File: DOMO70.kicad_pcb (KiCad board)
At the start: 2 copper layers, 148 parts, among them SW1 Rotary_Encoder_Switch, SW2 Rotary_Encoder_Switch, U1 OLED-SSD1306-OLED-SSD1306-4pi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, U2 proton_c

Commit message: Created speaker footprint/symbol
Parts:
- added D45: 1N4148, cftkb:D_DO-35_SOD27_P5.08mm_Horizontal, F.Cu at (232.4, 71.1)
- added D57: 1N4148, cftkb:D_DO-35_SOD27_P5.08mm_Horizontal, F.Cu at (232.4, 74.7)
- added D74: 1N4148, cftkb:D_DO-35_SOD27_P5.08mm_Horizontal, F.Cu at (241.1, 71.1)
- added MX56: MX-NoLED, MX_Only:MXOnly-1U-NoLED, F.Cu at (221.6, 68.9)
- added U2: AST1109MLTRQ, Buzzer_Beeper:Buzzer_Mallory_AST1109MLTRQ, F.Cu at (240.1, 64.1)
- renumbered D66 to D10, D67 to D11, D68 to D12, D69 to D13, D70 to D14, D71 to D15, D10 to D16, D11 to D17, D12 to D18, D13 to D19, D14 to D20, D15 to D21, D16 to D22, D17 to D23, D18 to D24, D59 to D25, D60 to D26, D61 to D27, D62 to D28, D72 to D29, D63 to D30, D19 to D31, D20 to D32, D21 to D33, D22 to D34, D23 to D35, D24 to D36, D25 to D37, D26 to D38, D51 to D39, D52 to D40, D53 to D41, D54 to D42, D56 to D43, D57 to D44, D27 to D46, D28 to D47, D29 to D48, D30 to D49, D31 to D50, D32 to D51, D33 to D52, D34 to D53, D47 to D54, D48 to D55, D49 to D56, D41 to D58, D50 to D59, D35 to D60, D36 to D61, D37 to D62, D38 to D63, D65 to D64, D39 to D65, D40 to D66, D58 to D67, D55 to D68, D46 to D69, D42 to D70, D43 to D71, D44 to D72, D45 to D73, MX66 to MX10, MX67 to MX11, MX68 to MX12, MX69 to MX13, MX70 to MX14, MX71 to MX15, MX10 to MX16, MX11 to MX17, MX12 to MX18, MX13 to MX19, MX14 to MX20, MX15 to MX21, MX16 to MX22, MX17 to MX23, MX18 to MX24, MX59 to MX25, MX60 to MX26, MX61 to MX27, MX62 to MX28, MX72 to MX29, MX63 to MX30, MX19 to MX31, MX20 to MX32, MX21 to MX33, MX22 to MX34, MX23 to MX35, MX24 to MX36, MX25 to MX37, MX26 to MX38, MX51 to MX39, MX52 to MX40, MX53 to MX41, MX54 to MX42, MX56 to MX43, MX57 to MX44, MX27 to MX45, MX28 to MX46, MX29 to MX47, MX30 to MX48, MX31 to MX49, MX32 to MX50, MX33 to MX51, MX34 to MX52, MX47 to MX53, MX48 to MX54, MX49 to MX55, MX41 to MX57, MX50 to MX58, MX35 to MX59, MX36 to MX60, MX37 to MX61, MX38 to MX62, MX65 to MX63, MX39 to MX64, MX40 to MX65, MX58 to MX66, MX55 to MX67, MX46 to MX68, MX42 to MX69, MX43 to MX70, MX44 to MX71, MX45 to MX72, U2 to U3
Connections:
- D10 pad 1: ROW8 -> ROW0
- D11 pad 1: ROW8 -> ROW0
- D12 pad 1: ROW8 -> ROW0
- D13 pad 1: ROW8 -> ROW0
- D14 pad 1: ROW8 -> ROW0
- D15 pad 1: ROW8 -> ROW0
- D25 pad 1: ROW7 -> ROW1
- D26 pad 1: ROW7 -> ROW1
- D27 pad 1: ROW7 -> ROW1
- D28 pad 1: ROW7 -> ROW1
- D29 pad 1: ROW8 -> ROW1
- D30 pad 1: ROW7 -> ROW1
- D39 pad 1: ROW6 -> ROW2
- D40 pad 1: ROW6 -> ROW2
- D41 pad 1: ROW6 -> ROW2
- D42 pad 1: ROW6 -> ROW2
- D43 pad 1: ROW6 -> ROW2
- D44 pad 1: ROW6 -> ROW2
- D54 pad 1: ROW5 -> ROW3
- D55 pad 1: ROW5 -> ROW3
- D56 pad 1: ROW5 -> ROW3
- D58 pad 1: ROW4 -> ROW3
- D59 pad 1: ROW5 -> ROW3
- D64 pad 1: ROW7 -> ROW4
- D64 pad 2: Net-(D65-Pad2) (its old number) -> Net-(D64-Pad2)
- D67 pad 1: ROW6 -> ROW4
- D68 pad 1: ROW6 -> ROW4
- D69 pad 1: ROW5 -> ROW4
- D71 pad 1: ROW5 -> ROW4
- D72 pad 1: ROW5 -> ROW4
- D73 pad 1: ROW5 -> ROW4
- MX10 pad 1: COL0 -> COL9
- MX11 pad 1: COL1 -> COL10
- MX12 pad 1: COL2 -> COL11
- MX13 pad 1: COL3 -> COL12
- MX14 pad 1: COL4 -> COL13
- MX15 pad 1: COL5 -> COL14
- MX25 pad 1: COL0 -> COL9
- MX26 pad 1: COL1 -> COL10
- MX27 pad 1: COL2 -> COL11
- MX28 pad 1: COL3 -> COL12
- MX29 pad 1: COL6 -> COL13
- MX30 pad 1: COL4 -> COL14
- MX39 pad 1: COL0 -> COL8
- MX40 pad 1: COL1 -> COL9
- MX41 pad 1: COL2 -> COL10
- MX42 pad 1: COL3 -> COL11
- MX43 pad 1: COL5 -> COL12
- MX44 pad 1: COL6 -> COL13
- MX53 pad 1: COL4 -> COL8
- MX54 pad 1: COL5 -> COL9
- MX55 pad 1: COL6 -> COL10
- MX57 pad 1: COL6 -> COL12
- MX58 pad 1: COL7 -> COL13
- MX63 pad 1: COL6 -> COL4
- MX63 pad 2: Net-(D65-Pad2) (its old number) -> Net-(D64-Pad2)
- MX64 pad 1: COL4 -> COL5
- MX65 pad 1: COL5 -> COL6
- MX66 pad 1: COL7 -> Net-(MX66-Pad1)
- MX67 pad 1: COL4 -> Net-(MX67-Pad1)
- MX68 pad 1: COL3 -> Net-(MX68-Pad1)
- MX69 pad 1: COL7 -> COL10
- MX70 pad 1: COL0 -> COL11
- MX71 pad 1: COL1 -> COL12
- MX72 pad 1: COL2 -> COL13
- SW1 pad S1: ROW7 -> Net-(D45-Pad2)
- SW1 pad S2: COL7 -> COL14
- SW2 pad S1: ROW8 -> Net-(D74-Pad2)
- SW2 pad S2: COL7 -> COL14
- U3 pad A10: Net-(U2-PadA10) -> COL13
- U3 pad A13: COL3 -> COL7
- U3 pad A14: COL2 -> COL6
- U3 pad A4: Net-(U2-PadA4) -> SPK
- U3 pad A8: Net-(U2-PadA8) -> COL8
- U3 pad A9: Net-(U2-PadA9) -> COL14
- U3 pad B10: ROW8 -> COL3
- U3 pad B11: COL0 -> COL4
- U3 pad B12: COL1 -> COL5
- U3 pad B14: ROW5 -> COL0
- U3 pad B15: ROW6 -> COL1
- U3 pad B2: COL7 -> COL9
- U3 pad B3: COL6 -> COL10
- U3 pad B4: COL5 -> COL11
- U3 pad B5: COL4 -> COL12
- U3 pad B9: ROW7 -> COL2
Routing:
- net GND: track 0.00 -> 1.66 mm

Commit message: Added routing
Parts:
- removed the D64 at (148.0, -58.9)
- removed the D64 at (106.6, -64.8)
- removed D73, D74: 1N4148, cftkb:D_DO-35_SOD27_P5.08mm_Horizontal
- removed the MX64 at (-75.9, -27.0)
- removed the MX64 at (-175.7, -0.44)
- added D64: 1N4148, cftkb:D_DO-35_SOD27_P5.08mm_Horizontal, B.Cu at (259.6, 130.2)
- added DE1: 1N4148, cftkb:D_DO-35_SOD27_P5.08mm_Horizontal, B.Cu at (354.0, 73.0)
- added DE2: 1N4148, cftkb:D_DO-35_SOD27_P5.08mm_Horizontal, B.Cu at (326.2, 73.0)
- added MX64: MX-NoLED, MX_Only:MXOnly-1.25U-NoLED, F.Cu at (250.0, 126.2)
- added MX_14: ExtraMX, MX_Only:MXOnly-2U-NoLED, F.Cu at (290.5, 50.0)
- added MX_29: ExtraMX, MX_Only:MXOnly-ISO-ReversedStabilizers, F.Cu at (297.7, 78.6)
- added MX_31: ExtraMX, MX_Only:MXOnly-1.25U-NoLED, F.Cu at (35.7, 88.1)
- added MX_43: ExtraMX, MX_Only:MXOnly-1U-NoLED, F.Cu at (276.2, 88.1)
- added MX_56: ExtraMX, MX_Only:MXOnly-1.75U-NoLED, F.Cu at (273.8, 107.2)
- added MX_59: ExtraMX, MX_Only:MXOnly-1.5U-NoLED, F.Cu at (38.1, 126.2)
- added MX_60: ExtraMX, MX_Only:MXOnly-1U-NoLED, F.Cu at (61.9, 126.2)
- added MX_61: ExtraMX, MX_Only:MXOnly-1.5U-NoLED, F.Cu at (85.7, 126.2)
- added MX_62: ExtraMX, MX_Only:MXOnly-7U-ReversedStabilizers-NoLED, F.Cu at (166.7, 126.2)
- added MX_64: ExtraMX, MX_Only:MXOnly-1.5U-NoLED, F.Cu at (247.7, 126.2)
- added MX_65: ExtraMX, MX_Only:MXOnly-1U-NoLED, F.Cu at (271.5, 126.2)
- added MX_66: ExtraMX, MX_Only:MXOnly-1.5U-NoLED, F.Cu at (295.3, 126.2)
- added U4: AST1109MLTRQ, Buzzer_Beeper:Buzzer_Mallory_AST1109MLTRQ, B.Cu at (192.1, 126.2)
- D24, D45, D57, D9: moved to B.Cu
- MX29: footprint MX_Only:MXOnly-1U-NoLED -> MX_Only:MXOnly-1.5U-NoLED
- MX31: footprint MX_Only:MXOnly-1U-NoLED -> MX_Only:MXOnly-1.75U-NoLED
- MX43, MX45: footprint MX_Only:MXOnly-1U-NoLED -> MX_Only:MXOnly-2.25U-NoLED
- MX56: footprint MX_Only:MXOnly-1U-NoLED -> MX_Only:MXOnly-2.75U-NoLED
- MX59, MX60, MX61, MX63, MX65, MX66: footprint MX_Only:MXOnly-1U-NoLED -> MX_Only:MXOnly-1.25U-NoLED
- MX62: footprint MX_Only:MXOnly-1U-NoLED -> MX_Only:MXOnly-6.25U-ReversedStabilizers-NoLED
- U1: value OLED-SSD1306-OLED-SSD1306-4pin-128x32 -> proton_c; footprint OLED-SSD1306-4pin-128x32:OLED-1306-Supports -> proton_c:proton_c; moved to B.Cu
- U2: value AST1109MLTRQ -> OLED-SSD1306-OLED-SSD1306-4pin-128x32; footprint Buzzer_Beeper:Buzzer_Mallory_AST1109MLTRQ -> OLED-SSD1306-4pin-128x32:OLED-1306-Supports
- U3: value proton_c -> AST1109MLTRQ; footprint proton_c:proton_c -> Buzzer_Beeper:Buzzer_Mallory_AST1109MLTRQ; moved to B.Cu
- moved MX58 511.9 mm to (357.2, 88.1)
- moved MX69 504.7 mm to (357.2, 107.2)
- moved MX15 475.8 mm to (300.0, 50.0)
- moved MX66 460.4 mm to (297.7, 126.2)
- moved D24 457.0 mm to (203.2, 73.0), turned to 90 degrees
- moved MX44 454.8 mm to (338.1, 88.1)
- moved MX57 450.0 mm to (300.0, 107.2)
- moved D9 448.4 mm to (193.7, 54.0), turned to 90 degrees
- moved MX43 444.5 mm to (288.1, 88.1)
- moved MX67 440.3 mm to (319.1, 107.2)
- moved MX68 439.2 mm to (338.1, 107.2)
- moved MX9 435.9 mm to (185.7, 50.0)
- moved MX24 434.8 mm to (195.3, 69.1)
- moved MX29 422.7 mm to (295.3, 69.1)
- moved MX30 420.6 mm to (319.1, 88.1)
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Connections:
- D45 pad 1: ROW2 -> ROW3
- D59 pad 1: ROW3 -> ROW4
- MX45 pad 2: Net-(D46-Pad2) -> Net-(D45-Pad2)
- MX46 pad 2: Net-(D47-Pad2) -> Net-(D46-Pad2)
- MX47 pad 2: Net-(D48-Pad2) -> Net-(D47-Pad2)
- MX48 pad 2: Net-(D49-Pad2) -> Net-(D48-Pad2)
- MX49 pad 2: Net-(D50-Pad2) -> Net-(D49-Pad2)
- MX50 pad 2: Net-(D51-Pad2) -> Net-(D50-Pad2)
- MX51 pad 2: Net-(D52-Pad2) -> Net-(D51-Pad2)
- MX52 pad 2: Net-(D53-Pad2) -> Net-(D52-Pad2)
- MX53 pad 2: Net-(D54-Pad2) -> Net-(D53-Pad2)
- MX54 pad 2: Net-(D55-Pad2) -> Net-(D54-Pad2)
- MX55 pad 2: Net-(D56-Pad2) -> Net-(D55-Pad2)
- MX56 pad 2: Net-(D57-Pad2) -> Net-(D56-Pad2)
- MX57 pad 2: Net-(D58-Pad2) -> Net-(D57-Pad2)
- MX58 pad 2: Net-(D59-Pad2) -> Net-(D58-Pad2)
- MX59 pad 2: Net-(D60-Pad2) -> Net-(D59-Pad2)
- MX60 pad 2: Net-(D61-Pad2) -> Net-(D60-Pad2)
- MX61 pad 2: Net-(D62-Pad2) -> Net-(D61-Pad2)
- MX62 pad 2: Net-(D63-Pad2) -> Net-(D62-Pad2)
- MX63 pad 2: Net-(D64-Pad2) -> Net-(D63-Pad2)
- MX65 pad 2: Net-(D66-Pad2) -> Net-(D65-Pad2)
- MX66 pad 1: Net-(MX66-Pad1) -> COL7
- MX66 pad 2: Net-(D67-Pad2) -> Net-(D66-Pad2)
- MX67 pad 1: Net-(MX67-Pad1) -> COL8
- MX67 pad 2: Net-(D68-Pad2) -> Net-(D67-Pad2)
- MX68 pad 1: Net-(MX68-Pad1) -> COL9
- MX68 pad 2: Net-(D69-Pad2) -> Net-(D68-Pad2)
- MX69 pad 2: Net-(D70-Pad2) -> Net-(D69-Pad2)
- MX70 pad 2: Net-(D71-Pad2) -> Net-(D70-Pad2)
- MX71 pad 2: Net-(D72-Pad2) -> Net-(D71-Pad2)
- MX72 pad 2: Net-(D73-Pad2) -> Net-(D72-Pad2)
- SW1 pad S1: Net-(D45-Pad2) -> Net-(DE1-Pad2)
- U2 pad 1: SPK -> SDA
- U2 pad 2: GND -> SCL
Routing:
- net ROW4: track 0.00 -> 452.4 mm, vias 0 -> 1
- net COL0: track 0.00 -> 394.1 mm
- net COL1: track 0.00 -> 370.4 mm
- net ROW2: track 0.00 -> 363.4 mm, vias 0 -> 1
- net ROW3: track 0.00 -> 354.7 mm, vias 0 -> 1
- net COL2: track 0.00 -> 346.8 mm
- net ROW1: track 0.00 -> 321.6 mm, vias 0 -> 2
- net COL3: track 0.00 -> 317.9 mm, vias 0 -> 1
- net COL4: track 0.00 -> 299.7 mm, vias 0 -> 1
- net ROW0: track 0.00 -> 295.5 mm
- net GND: track 1.66 -> 285.5 mm, vias 0 -> 1
- net COL5: track 0.00 -> 278.0 mm
- net SPK: track 0.00 -> 263.6 mm, vias 0 -> 2
- net COL6: track 0.00 -> 258.2 mm
- net COL7: track 0.00 -> 244.0 mm, vias 0 -> 1
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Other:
- board outline added: 342.9 x 95.2 mm
- net class Default: clearance 0.2 -> 0.3
- net class Power added: clearance 0.3, trace_width 0.381, via_dia 0.8, via_drill 0.4
- rule trace_clearance: 0.2 -> 0.3

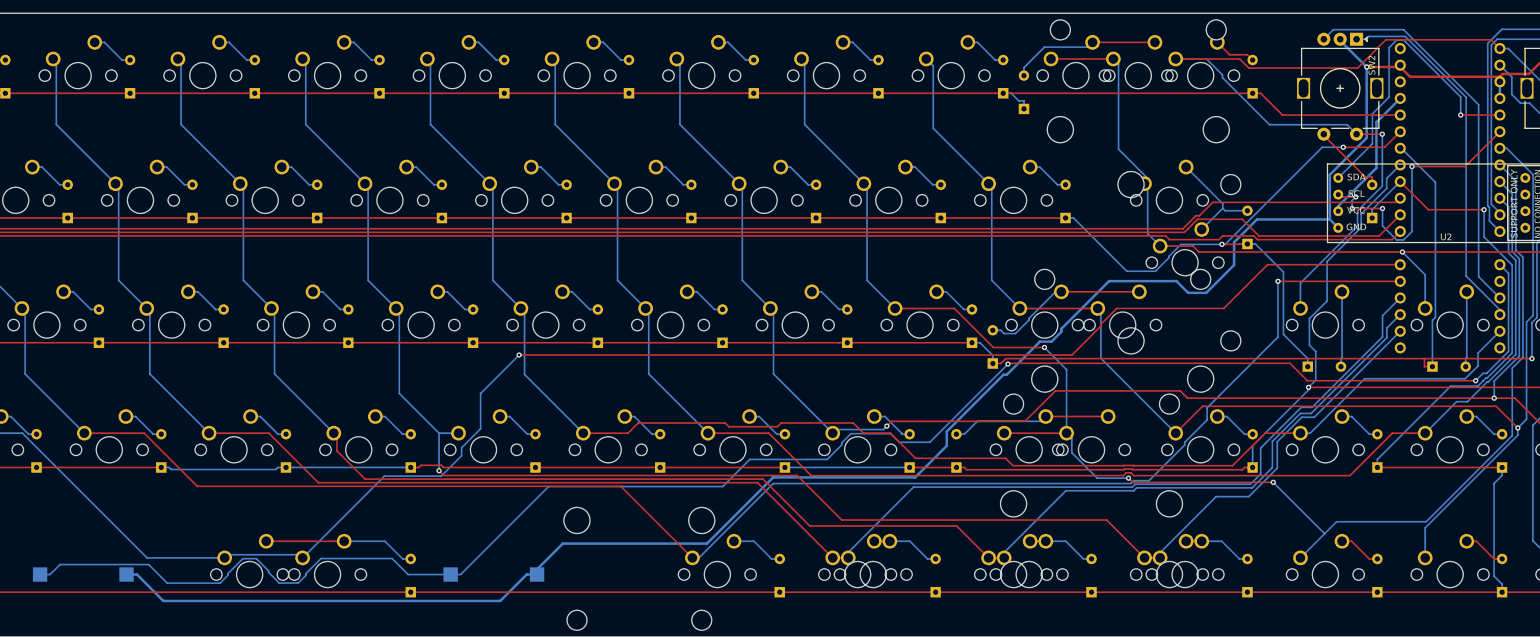
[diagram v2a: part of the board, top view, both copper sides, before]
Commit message: Added more routing
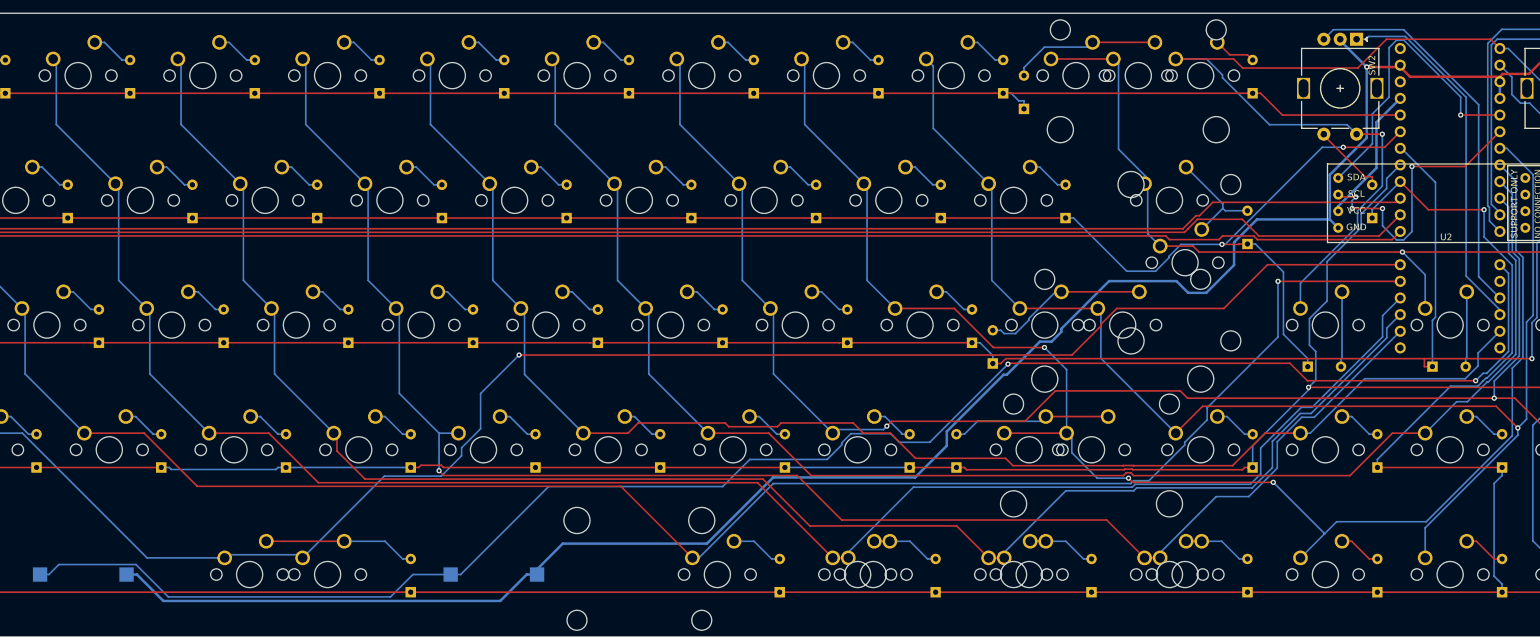
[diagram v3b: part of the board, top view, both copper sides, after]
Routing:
- net SPK: track 263.6 -> 259.8 mm
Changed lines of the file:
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@@
     (thickness 1.6)
     (drawings 8)
-    (tracks 979)
+    (tracks 968)
     (zones 0)
     (modules 164)
@@
   (segment (start 347.0185 45.8688) (end 345.738 45.8688) (width 0.25) (layer B.Cu) (net 100))
   (via (at 327.7822 58.95) (size 0.8) (layers F.Cu B.Cu) (net 100))
-  (segment (start 344.4036 44.5344) (end 345.738 45.8688) (width 0.25) (layer F.Cu) (net 100))
-  (segment (start 328.3236 44.5344) (end 344.4036 44.5344) (width 0.25) (layer F.Cu) (net 100))
-  (segment (start 324.007999 48.850001) (end 328.3236 44.5344) (width 0.25) (layer F.Cu) (net 100))
-  (segment (start 307.386999 48.850001) (end 324.007999 48.850001) (width 0.25) (layer F.Cu) (net 100))
-  (segment (start 306.003198 47.4662) (end 307.386999 48.850001) (width 0.25) (layer F.Cu) (net 100))
-  (segment (start 296.228 47.4662) (end 306.003198 47.4662) (width 0.25) (layer F.Cu) (net 100))
+  (segment (start 344.888001 45.018801) (end 345.738 45.8688) (width 0.25) (layer F.Cu) (net 100))
+  (segment (start 344.3192 44.45) (end 344.888001 45.018801) (width 0.25) (layer F.Cu) (net 100))
+  (segment (start 328.424298 44.45) (end 344.3192 44.45) (width 0.25) (layer F.Cu) (net 100))
+  (segment (start 324.024297 48.850001) (end 328.424298 44.45) (width 0.25) (layer F.Cu) (net 100))
+  (segment (start 306.456252 48.850001) (end 324.024297 48.850001) (width 0.25) (layer F.Cu) (net 100))
+  (segment (start 305.072451 47.4662) (end 306.456252 48.850001) (width 0.25) (layer F.Cu) (net 100))
+  (segment (start 296.228 47.4662) (end 305.072451 47.4662) (width 0.25) (layer F.Cu) (net 100))
   (segment (start 342.0369 96.6082) (end 316.3395 96.6082) (width 0.25) (layer F.Cu) (net 101))
   (segment (start 316.3395 96.6082) (end 313.672 93.9407) (width 0.25) (layer F.Cu) (net 101))
@@
   (segment (start 258.6659 106.0057) (end 270.6053 94.0663) (width 0.25) (layer B.Cu) (net 101))
   (segment (start 185.488 126.206) (end 187.0133 126.206) (width 0.25) (layer B.Cu) (net 101))
-  (segment (start 124.3063 126.206) (end 125.8316 124.6807) (width 0.25) (layer B.Cu) (net 101))
-  (segment (start 125.8316 124.6807) (end 139.3616 124.6807) (width 0.25) (layer B.Cu) (net 101))
-  (segment (start 139.3616 124.6807) (end 142.1996 127.5187) (width 0.25) (layer B.Cu) (net 101))
-  (segment (start 142.1996 127.5187) (end 150.2764 127.5187) (width 0.25) (layer B.Cu) (net 101))
-  (segment (start 150.2764 127.5187) (end 151.4687 126.3264) (width 0.25) (layer B.Cu) (net 101))
-  (segment (start 151.4687 126.3264) (end 151.4687 126.0715) (width 0.25) (layer B.Cu) (net 101))
-  (segment (start 151.4687 126.0715) (end 153.7538 123.7864) (width 0.25) (layer B.Cu) (net 101))
-  (segment (start 153.7538 123.7864) (end 155.8105 123.7864) (width 0.25) (layer B.Cu) (net 101))
-  (segment (start 155.8105 123.7864) (end 157.6853 125.6612) (width 0.25) (layer B.Cu) (net 101))
-  (segment (start 157.6853 125.6612) (end 157.6853 125.8846) (width 0.25) (layer B.Cu) (net 101))
-  (segment (start 157.6853 125.8846) (end 159.3071 127.5064) (width 0.25) (layer B.Cu) (net 101))
-  (segment (start 159.3071 127.5064) (end 162.21 127.5064) (width 0.25) (layer B.Cu) (net 101))
-  (segment (start 162.21 127.5064) (end 163.3757 126.3407) (width 0.25) (layer B.Cu) (net 101))
-  (segment (start 163.3757 126.3407) (end 163.3757 126.0715) (width 0.25) (layer B.Cu) (net 101))
-  (segment (start 163.3757 126.0715) (end 165.6896 123.7576) (width 0.25) (layer B.Cu) (net 101))
-  (segment (start 165.6896 123.7576) (end 176.5386 123.7576) (width 0.25) (layer B.Cu) (net 101))
-  (segment (start 176.5386 123.7576) (end 178.987 126.206) (width 0.25) (layer B.Cu) (net 101))
-  (segment (start 178.987 126.206) (end 185.488 126.206) (width 0.25) (layer B.Cu) (net 101))
   (segment (start 342.0369 96.6082) (end 343.1673 95.4778) (width 0.25) (layer B.Cu) (net 101))
   (segment (start 343.1673 95.4778) (end 343.7235 95.4778) (width 0.25) (layer B.Cu) (net 101))
@@
   (segment (start 347.059 92.1423) (end 347.059 80.2098) (width 0.25) (layer B.Cu) (net 101))
   (segment (start 347.059 80.2098) (end 345.738 78.8888) (width 0.25) (layer B.Cu) (net 101))
-  (segment (start 122.781 126.206) (end 124.3063 126.206) (width 0.25) (layer B.Cu) (net 101))
   (via (at 342.0369 96.6082) (size 0.8) (layers F.Cu B.Cu) (net 101))
   (via (at 270.6053 94.0663) (size 0.8) (layers F.Cu B.Cu) (net 101))
+  (segment (start 124.131 126.206) (end 122.781 126.206) (width 0.25) (layer B.Cu) (net 101))
+  (segment (start 125.656001 124.680999) (end 124.131 126.206) (width 0.25) (layer B.Cu) (net 101))
+  (segment (start 137.421001 124.680999) (end 125.656001 124.680999) (width 0.25) (layer B.Cu) (net 101))
+  (segment (start 142.364292 129.62429) (end 137.421001 124.680999) (width 0.25) (layer B.Cu) (net 101))
+  (segment (start 176.303708 129.62429) (end 142.364292 129.62429) (width 0.25) (layer B.Cu) (net 101))
+  (segment (start 179.721998 126.206) (end 176.303708 129.62429) (width 0.25) (layer B.Cu) (net 101))
+  (segment (start 185.488 126.206) (end 179.721998 126.206) (width 0.25) (layer B.Cu) (net 101))
   (segment (start 354.012 66.675) (end 354.012 59.981) (width 0.25) (layer B.Cu) (net 102))
   (segment (start 354.012 59.981) (end 352.981 58.95) (width 0.25) (layer B.Cu) (net 102))

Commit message: Updating who-knows-what
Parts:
- moved D72 56.8 mm to (310.4, 145.3)
- moved D58 53.5 mm to (314.3, 108.7), turned to 0 degrees
- moved D68 53.5 mm to (295.3, 127.8), turned to 0 degrees
- moved D69 53.5 mm to (314.3, 127.8), turned to 0 degrees
- moved D67 53.5 mm to (276.2, 127.8), turned to 0 degrees
- moved D30 41.4 mm to (276.2, 108.7)
- moved D44 41.4 mm to (295.3, 108.7)
- moved D65 40.9 mm to (244.5, 142.9)
- moved MX56 40.9 mm to (244.5, 119.9)
- moved D14 40.9 mm to (234.2, 69.1)
- moved D29 40.9 mm to (268.3, 89.7)
- moved D36 40.9 mm to (111.9, 104.8)
- moved D38 40.9 mm to (150.0, 104.8)
- moved D40 40.9 mm to (188.1, 104.8)
- moved D41 40.9 mm to (207.2, 104.8)
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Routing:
- net ROW4: track 452.4 -> 0.00 mm, vias 1 -> 0
- net COL0: track 394.1 -> 0.00 mm
- net COL1: track 370.4 -> 0.00 mm
- net ROW2: track 363.4 -> 0.00 mm, vias 1 -> 0
- net ROW3: track 354.7 -> 0.00 mm, vias 1 -> 0
- net COL2: track 346.8 -> 0.00 mm
- net ROW1: track 321.6 -> 0.00 mm, vias 2 -> 0
- net COL3: track 317.9 -> 0.00 mm, vias 1 -> 0
- net COL4: track 299.7 -> 0.00 mm, vias 1 -> 0
- net ROW0: track 295.5 -> 0.00 mm
- net GND: track 285.5 -> 0.00 mm, vias 1 -> 0
- net COL5: track 278.0 -> 0.00 mm
- net SPK: track 259.8 -> 0.00 mm, vias 2 -> 0
- net COL6: track 258.2 -> 0.00 mm
- net COL7: track 244.0 -> 0.00 mm, vias 1 -> 0
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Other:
- board size 342.9 x 95.2 mm -> 342.9 x 95.3 mm
- board text added: "Designed By Dom Ruggeri 2019"

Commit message: Added routes, graphics
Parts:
- added G***: LOGO, Images:BeezerBike, F.Cu at (288.9, 95.2)
- added G***: LOGO, Images:BeezerWindowNeg, B.Cu at (135.6, 80.6)
- moved D30 24.5 mm to (265.5, 86.7)
- moved D44 24.5 mm to (284.5, 86.7)
- moved D58 24.4 mm to (315.5, 84.3), turned to 90 degrees
- moved D67 24.4 mm to (277.4, 103.4), turned to 90 degrees
- moved D68 24.4 mm to (296.4, 103.4), turned to 90 degrees
- moved D69 24.4 mm to (315.5, 103.4), turned to 90 degrees
- moved D72 23.4 mm to (315.5, 122.4)
- moved MX29 23.1 mm to (245.6, 61.3)
- moved D57 23.1 mm to (258.3, 103.4)
- moved D70 23.1 mm to (277.4, 122.4)
- moved MX30 23.1 mm to (269.4, 80.4)
- moved MX44 23.1 mm to (288.5, 80.4)
- moved MX70 23.1 mm to (269.4, 118.5)
- moved MX71 23.1 mm to (288.5, 118.5)
- moved MX_66 23.1 mm to (245.6, 118.5)
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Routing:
- net ROW4: track 0.00 -> 452.4 mm, vias 0 -> 1
- net COL0: track 0.00 -> 394.1 mm
- net COL1: track 0.00 -> 370.4 mm
- net ROW2: track 0.00 -> 363.4 mm, vias 0 -> 1
- net ROW3: track 0.00 -> 354.7 mm, vias 0 -> 1
- net COL2: track 0.00 -> 346.8 mm
- net ROW1: track 0.00 -> 321.6 mm, vias 0 -> 2
- net COL3: track 0.00 -> 317.9 mm, vias 0 -> 1
- net COL4: track 0.00 -> 299.7 mm, vias 0 -> 1
- net ROW0: track 0.00 -> 295.5 mm
- net GND: track 0.00 -> 285.5 mm, vias 0 -> 1
- net COL5: track 0.00 -> 278.0 mm
- net SPK: track 0.00 -> 263.6 mm, vias 0 -> 2
- net COL6: track 0.00 -> 258.2 mm
- net COL7: track 0.00 -> 244.0 mm, vias 0 -> 1
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
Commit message: More graphics
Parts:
- added G***: LOGO, Images:logo, F.Cu at (12.1, 75.4)
